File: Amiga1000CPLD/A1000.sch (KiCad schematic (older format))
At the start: 11 parts, among them J1 Raspberry_Pi_2_3, U1 DeniseSocket, U2 DenisePins, U3 XC9572VQ44

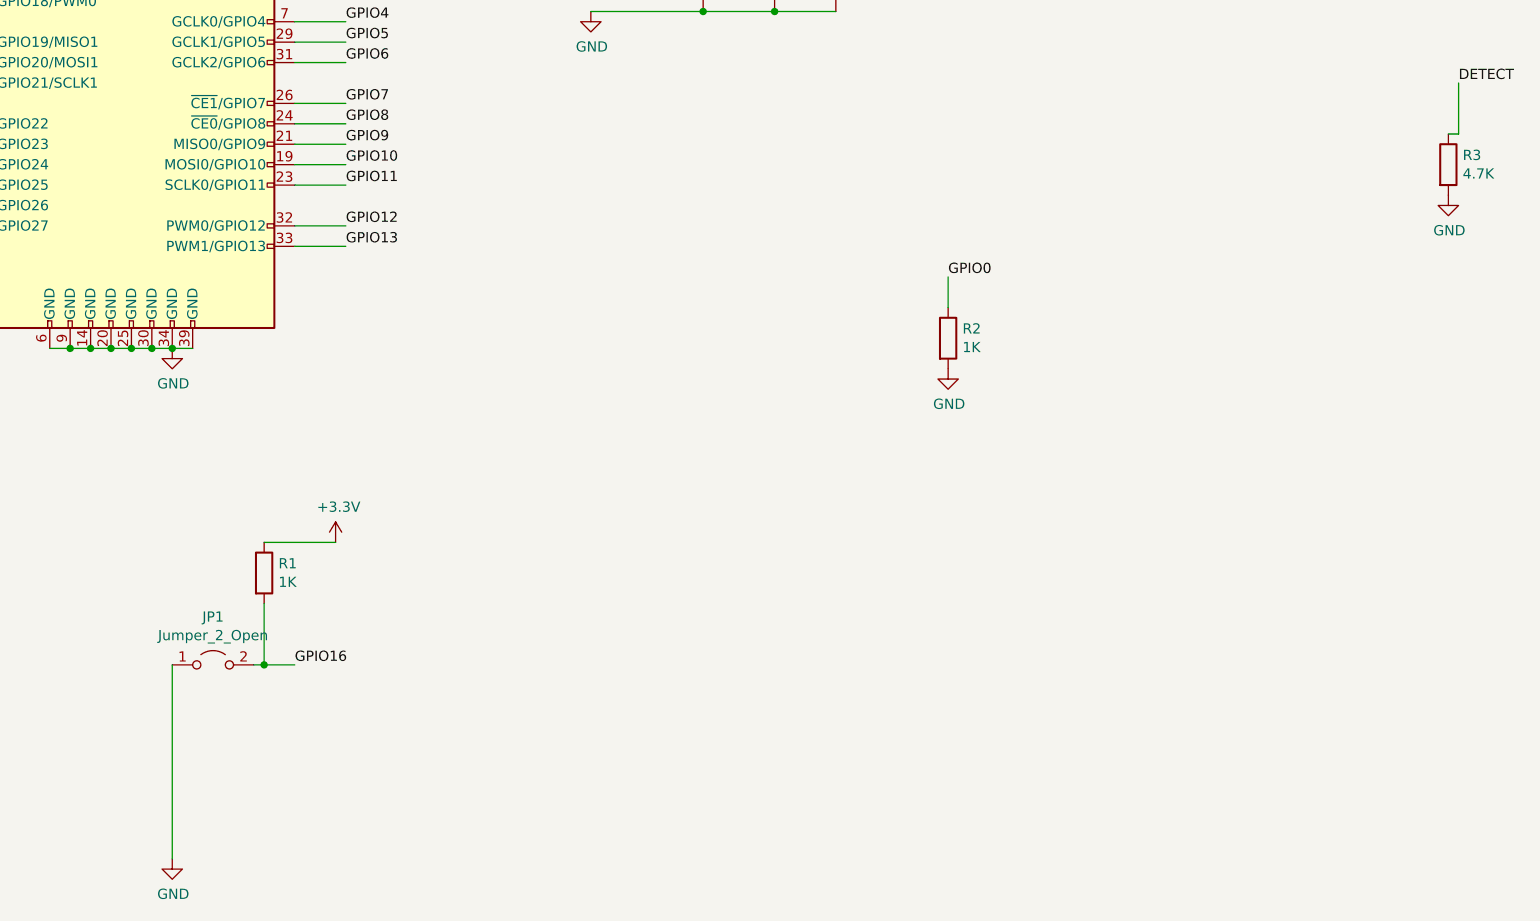
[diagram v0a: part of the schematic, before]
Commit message: Update Amiga 1000 and READMEs
Changes to Amiga 1000 based on feedback:
* Added a CSYNC hook pin
* Added optional buttons 2 & 3

Also moved the buttons to the side as there is more space there.

A2000 README updated as Beta20 software includes the profiles.
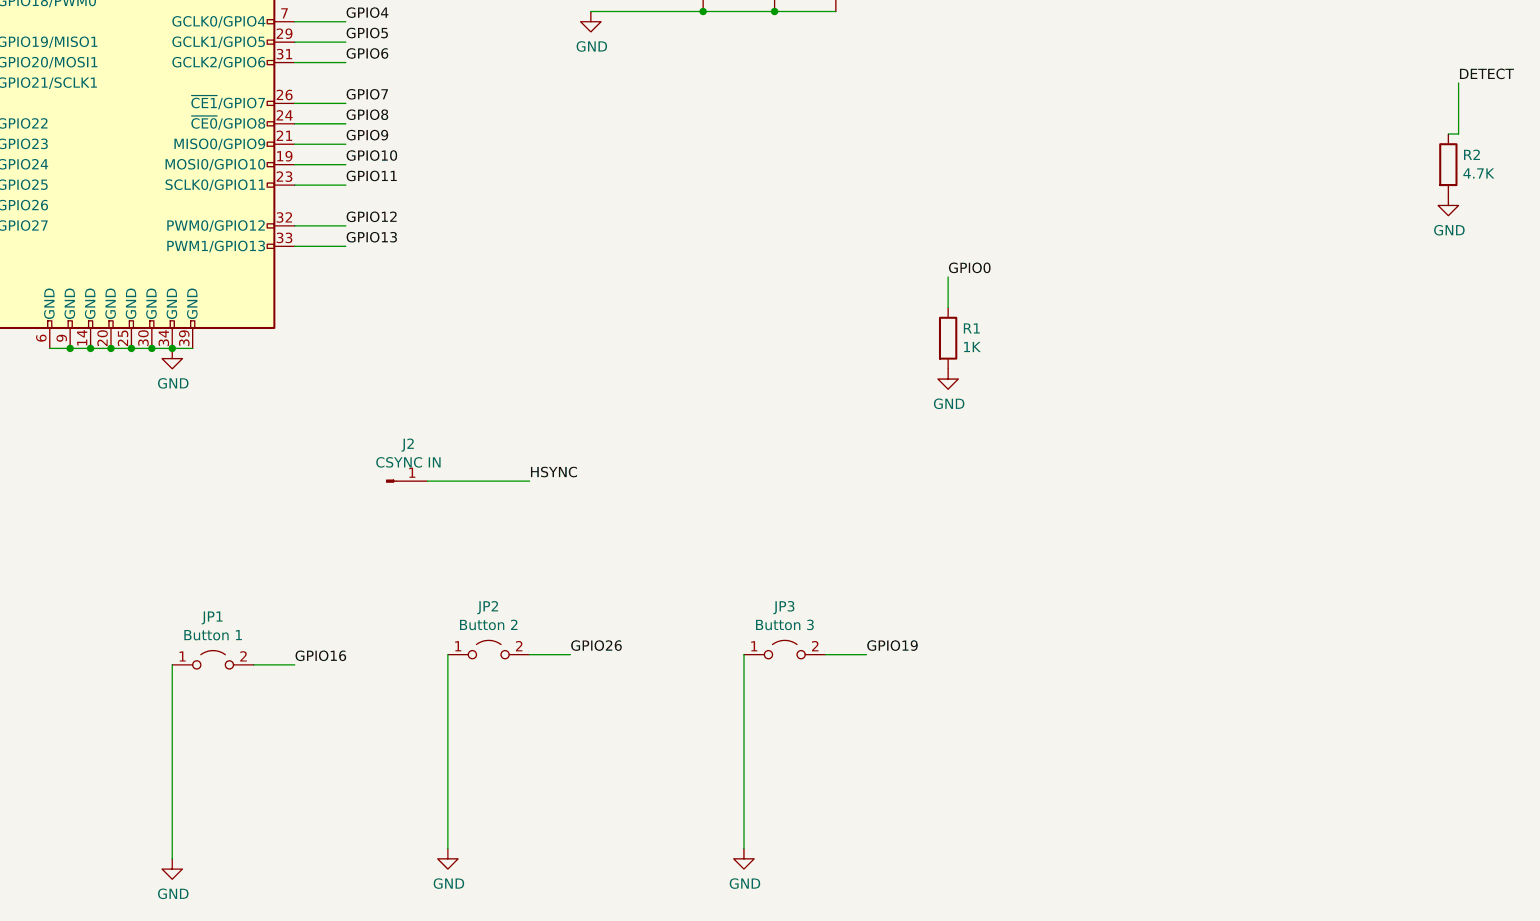
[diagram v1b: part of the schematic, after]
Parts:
- removed R1: 1K, Resistor_SMD:R_0603_1608Metric_Pad0.98x0.95mm_HandSolder, symbol Device:R
- added J2: CSYNC IN, Connector_PinHeader_2.54mm:PinHeader_1x01_P2.54mm_Horizontal, symbol Connector:Conn_01x01_Male
- added JP2: Button 2, Connector_PinHeader_2.54mm:PinHeader_1x02_P2.54mm_Horizontal, symbol Jumper:Jumper_2_Open
- added JP3: Button 3, Connector_PinHeader_2.54mm:PinHeader_1x02_P2.54mm_Horizontal, symbol Jumper:Jumper_2_Open
- JP1: value Jumper_2_Open -> Button 1
- renumbered R2 to R1, R3 to R2
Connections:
- net GND: now also JP2.1 (A), JP3.1 (A)
- net GPIO19: now also JP3.2 (B)
- net GPIO26: now also JP2.2 (B)
- net HSYNC: now also J2.1 (Pin_1)
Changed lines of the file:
@@
 	2950 6400 2750 6400
-$Comp
-L Device:R R1
-U 1 1 609E3D42
-P 6250 8400
-F 0 "R1" H 6320 8446 50  0000 L CNN
-F 1 "1K" H 6320 8355 50  0000 L CNN
-F 2 "Resistor_SMD:R_0603_1608Metric_Pad0.98x0.95mm_HandSolder" V 6180 8400 50  0001 C CNN
-F 3 "~" H 6250 8400 50  0001 C CNN
-	1    6250 8400
-	1    0    0    -1
-$EndComp
 $Comp
 L Jumper:Jumper_2_Open JP1
@@
 P 6000 8850
 F 0 "JP1" H 6000 9085 50  0000 C CNN
-F 1 "Jumper_2_Open" H 6000 8994 50  0000 C CNN
+F 1 "Button 1" H 6000 8994 50  0000 C CNN
 F 2 "Connector_PinHeader_2.54mm:PinHeader_1x02_P2.54mm_Horizontal" H 6000 8850 50  0001 C CNN
 F 3 "~" H 6000 8850 50  0001 C CNN
@@
 	1    0    0    -1
 $EndComp
-Wire Wire Line
-	6250 8550 6250 8850
-Wire Wire Line
-	6250 8850 6200 8850
-$Comp
-L power:+3.3V #PWR09
-U 1 1 60AA7B16
-P 6600 8250
-F 0 "#PWR09" H 6600 8100 50  0001 C CNN
-F 1 "+3.3V" H 6615 8423 50  0000 C CNN
-F 2 "" H 6600 8250 50  0001 C CNN
-F 3 "" H 6600 8250 50  0001 C CNN
-	1    6600 8250
-	1    0    0    -1
-$EndComp
-Wire Wire Line
-	6600 8250 6250 8250
 $Comp
 L power:GND #PWR07
@@
 Text Label 6400 8850 0    50   ~ 0
 GPIO16
-Wire Wire Line
-	6400 8850 6250 8850
-Connection ~ 6250 8850
 $Comp
-L power:GND #PWR015
+L power:GND #PWR016
 U 1 1 605C942A
 P 12050 6550
-F 0 "#PWR015" H 12050 6300 50  0001 C CNN
+F 0 "#PWR016" H 12050 6300 50  0001 C CNN
 F 1 "GND" H 12055 6377 50  0000 C CNN
 F 2 "" H 12050 6550 50  0001 C CNN
@@
 DETECT
 $Comp
-L Device:R R3
+L Device:R R2
 U 1 1 607CB6C9
 P 12050 6400
-F 0 "R3" H 12120 6446 50  0000 L CNN
+F 0 "R2" H 12120 6446 50  0000 L CNN
 F 1 "4.7K" H 12120 6355 50  0000 L CNN
 F 2 "Resistor_SMD:R_0603_1608Metric_Pad0.98x0.95mm_HandSolder" V 11980 6400 50  0001 C CNN
@@
 	12100 6250 12050 6250
 $Comp
-L Device:R R2
+L Device:R R1
 U 1 1 60964FFF
 P 9600 7250
-F 0 "R2" H 9670 7296 50  0000 L CNN
+F 0 "R1" H 9670 7296 50  0000 L CNN
 F 1 "1K" H 9670 7205 50  0000 L CNN
 F 2 "Resistor_SMD:R_0603_1608Metric_Pad0.98x0.95mm_HandSolder" V 9530 7250 50  0001 C CNN
@@
 $EndComp
 $Comp
-L power:GND #PWR014
+L power:GND #PWR015
 U 1 1 6096572B
 P 9600 7400
-F 0 "#PWR014" H 9600 7150 50  0001 C CNN
+F 0 "#PWR015" H 9600 7150 50  0001 C CNN
 F 1 "GND" H 9605 7227 50  0000 C CNN
 F 2 "" H 9600 7400 50  0001 C CNN
@@
 Wire Wire Line
 	7850 5650 8400 5650
+Wire Wire Line
+	6200 8850 6400 8850
+$Comp
+L Jumper:Jumper_2_Open JP3
+U 1 1 609F5BB6
+P 8800 8800
+F 0 "JP3" H 8800 9035 50  0000 C CNN
+F 1 "Button 3" H 8800 8944 50  0000 C CNN
+F 2 "Connector_PinHeader_2.54mm:PinHeader_1x02_P2.54mm_Horizontal" H 8800 8800 50  0001 C CNN
+F 3 "~" H 8800 8800 50  0001 C CNN
+	1    8800 8800
+	1    0    0    -1
+$EndComp
+$Comp
+L power:GND #PWR014
+U 1 1 609F5BBC
+P 8600 9750
+F 0 "#PWR014" H 8600 9500 50  0001 C CNN
+F 1 "GND" H 8605 9577 50  0000 C CNN
+F 2 "" H 8600 9750 50  0001 C CNN
+F 3 "" H 8600 9750 50  0001 C CNN
+	1    8600 9750
+	1    0    0    -1
+$EndComp
+Text Label 9200 8800 0    50   ~ 0
+GPIO19
+Wire Wire Line
+	8600 8800 8600 9750
+Wire Wire Line
+	9000 8800 9200 8800
+$Comp
+L Jumper:Jumper_2_Open JP2
+U 1 1 60A0BE28
+P 7350 8800
+F 0 "JP2" H 7350 9035 50  0000 C CNN
+F 1 "Button 2" H 7350 8944 50  0000 C CNN
+F 2 "Connector_PinHeader_2.54mm:PinHeader_1x02_P2.54mm_Horizontal" H 7350 8800 50  0001 C CNN
+F 3 "~" H 7350 8800 50  0001 C CNN
+	1    7350 8800
+	1    0    0    -1
+$EndComp
+$Comp
+L power:GND #PWR09
+U 1 1 60A0BE2E
+P 7150 9750
+F 0 "#PWR09" H 7150 9500 50  0001 C CNN
+F 1 "GND" H 7155 9577 50  0000 C CNN
+F 2 "" H 7150 9750 50  0001 C CNN
+F 3 "" H 7150 9750 50  0001 C CNN
+	1    7150 9750
+	1    0    0    -1
+$EndComp
+Text Label 7750 8800 0    50   ~ 0
+GPIO26
+Wire Wire Line
+	7150 8800 7150 9750
+Wire Wire Line
+	7550 8800 7750 8800
+$Comp
+L Connector:Conn_01x01_Male J2
+U 1 1 60A2274B
+P 6850 7950
+F 0 "J2" H 6958 8131 50  0000 C CNN
+F 1 "CSYNC IN" H 6958 8040 50  0000 C CNN
+F 2 "Connector_PinHeader_2.54mm:PinHeader_1x01_P2.54mm_Horizontal" H 6850 7950 50  0001 C CNN
+F 3 "~" H 6850 7950 50  0001 C CNN
+	1    6850 7950
+	1    0    0    -1
+$EndComp
+Text Label 7550 7950 0    50   ~ 0
+HSYNC
+Wire Wire Line
+	7550 7950 7050 7950
 $EndSCHEMATC
